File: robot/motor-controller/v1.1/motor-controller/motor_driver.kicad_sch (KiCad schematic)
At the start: 76 parts, among them J2 BM03B-ACHFKS, J4 BM06B-ACHFKS, J6 Conn_ARM_JTAG_SWD_10, Q1 STL90N10F7, Q2 STL90N10F7, Q3 STL90N10F7, Q4 STL90N10F7, Q5 STL90N10F7, Q6 STL90N10F7, Q7 BSS138K, U1 STSPIN32F0B, Y1 Q13FC13500005, Y2 TAXM8M4RDBCCT2T

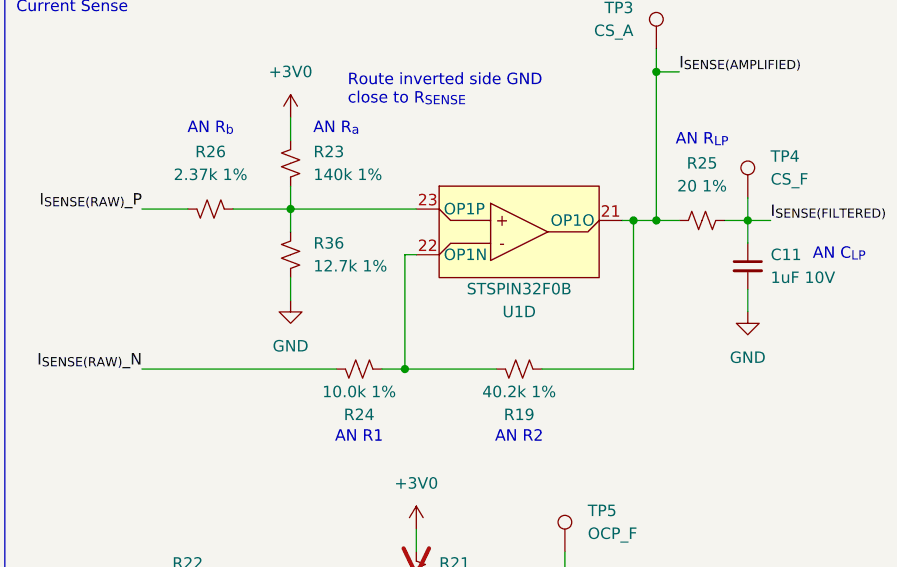
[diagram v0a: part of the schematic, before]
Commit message: fixed amplifier schematic
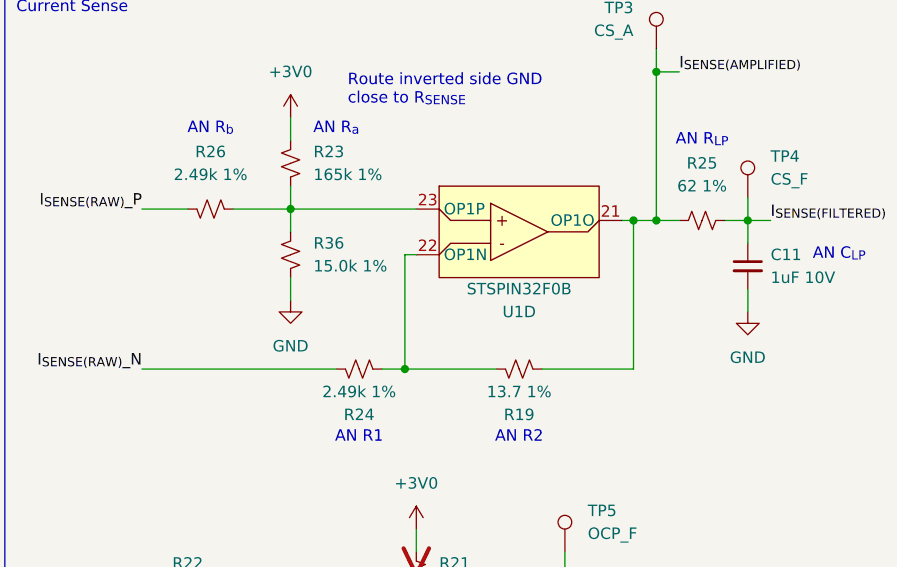
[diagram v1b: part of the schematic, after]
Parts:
- R19: value 40.2k 1% -> 13.7 1%
- R23: value 140k 1% -> 165k 1%
- R24: value 10.0k 1% -> 2.49k 1%
- R25: value 20 1% -> 62 1%
- R26: value 2.37k 1% -> 2.49k 1%
- R36: value 12.7k 1% -> 15.0k 1%
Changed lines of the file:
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@@
 			)
 		)
-		(property "Value" "20 1%"
+		(property "Value" "62 1%"
 			(at 316.23 168.91 90)
 			(effects
@@
 			)
 		)
-		(property "Value" "12.7k 1%"
+		(property "Value" "15.0k 1%"
 			(at 273.05 177.7999 0)
 			(effects
@@
 			)
 		)
-		(property "Value" "40.2k 1%"
+		(property "Value" "13.7 1%"
 			(at 295.91 191.77 90)
 			(effects
@@
 			)
 		)
-		(property "Value" "10.0k 1%"
+		(property "Value" "2.49k 1%"
 			(at 278.13 191.77 90)
 			(effects
@@
 			)
 		)
-		(property "Value" "2.37k 1%"
+		(property "Value" "2.49k 1%"
 			(at 261.62 167.64 90)
 			(effects
@@
 			)
 		)
-		(property "Value" "140k 1%"
+		(property "Value" "165k 1%"
 			(at 273.05 167.6399 0)
 			(effects

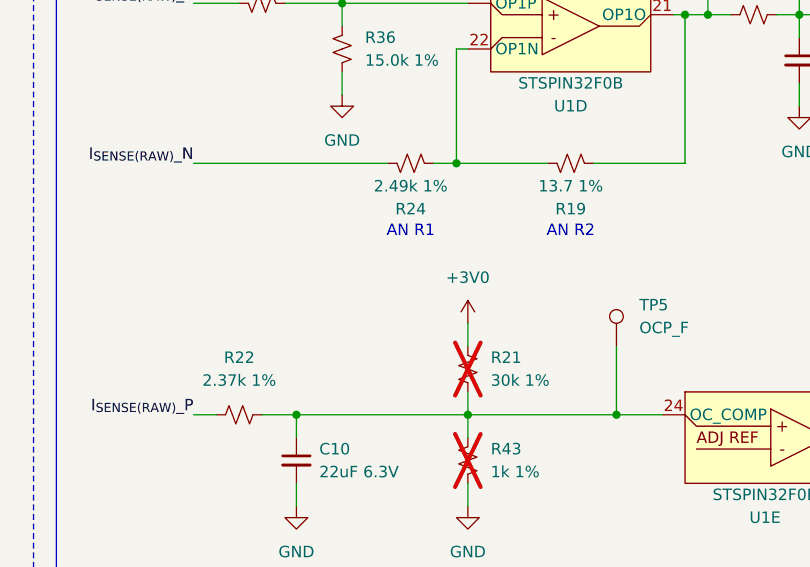
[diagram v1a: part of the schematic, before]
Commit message: BoM tweaks for prod
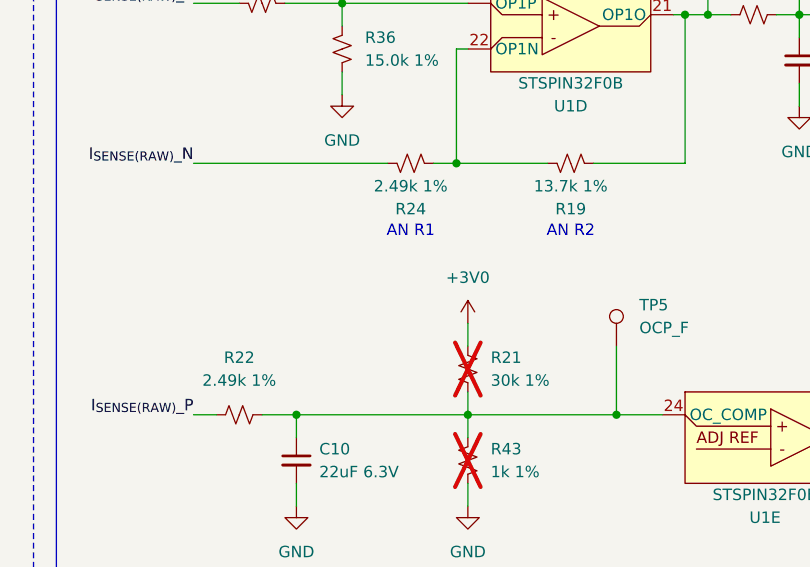
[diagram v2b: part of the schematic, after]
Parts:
- R19: value 13.7 1% -> 13.7k 1%
- R22: value 2.37k 1% -> 2.49k 1%
- TP1, TP2, TP3, TP4, TP5: now left out of the parts list
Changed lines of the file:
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@@
 		(unit 1)
 		(exclude_from_sim no)
-		(in_bom yes)
+		(in_bom no)
 		(on_board yes)
 		(dnp no)
@@
 		(unit 1)
 		(exclude_from_sim no)
-		(in_bom yes)
+		(in_bom no)
 		(on_board yes)
 		(dnp no)
@@
 			)
 		)
-		(property "Value" "2.37k 1%"
+		(property "Value" "2.49k 1%"
 			(at 259.08 213.36 90)
 			(effects
@@
 			)
 		)
-		(property "Value" "13.7 1%"
+		(property "Value" "13.7k 1%"
 			(at 295.91 191.77 90)
 			(effects
@@
 		(unit 1)
 		(exclude_from_sim no)
-		(in_bom yes)
+		(in_bom no)
 		(on_board yes)
 		(dnp no)
@@
 		(unit 1)
 		(exclude_from_sim no)
-		(in_bom yes)
+		(in_bom no)
 		(on_board yes)
 		(dnp no)
@@
 		(unit 1)
 		(exclude_from_sim no)
-		(in_bom yes)
+		(in_bom no)
 		(on_board yes)
 		(dnp no)

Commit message: BoM updated
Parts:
- C20, C21: LCSC C710643 -> C161525
- F4: LCSC (none) -> C377220
- J2: LCSC (none) -> C5177195
- J4: LCSC (none) -> C5304907
- R12, R13, R2, R3, R6, R9: LCSC C4962 -> C100501
- R19: LCSC C137983 -> C25854
- R21: LCSC C477764 -> C25776
- R22, R26: LCSC C25881 -> C25884
- R23: LCSC C852528 -> C38706
- R24: LCSC C60490 -> C25884
- R25: LCSC C138031 -> C100501
- R36: LCSC C852509 -> C2909322
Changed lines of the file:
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@@
 			)
 		)
+		(property "LCSC" "C5304907"
+			(at 182.88 176.53 0)
+			(effects
+				(font
+					(size 1.27 1.27)
+				)
+				(hide yes)
+			)
+		)
 		(pin "4"
 		)
@@
 			)
 		)
+		(property "LCSC" "C5177195"
+			(at 213.36 176.53 0)
+			(effects
+				(font
+					(size 1.27 1.27)
+				)
+				(hide yes)
+			)
+		)
 		(pin "2"
 		)
@@
 			)
 		)
-		(property "LCSC" "C4962"
+		(property "LCSC" "C100501"
 			(at 72.39 231.14 0)
 			(effects
@@
 			)
 		)
-		(property "LCSC" "C138031"
+		(property "LCSC" "C100501"
 			(at 316.23 166.37 0)
 			(effects
@@
 			)
 		)
-		(property "LCSC" "C25881"
+		(property "LCSC" "C25884"
 			(at 259.08 210.82 0)
 			(effects
@@
 			)
 		)
-		(property "LCSC" "C852509"
+		(property "LCSC" "C2909322"
 			(at 273.05 175.2599 0)
 			(effects
@@
 			)
 		)
-		(property "LCSC" "C137983"
+		(property "LCSC" "C25854"
 			(at 295.91 194.31 0)
 			(effects
@@
 			)
 		)
-		(property "LCSC" "C477764"
+		(property "LCSC" "C25776"
 			(at 287.02 210.8199 0)
 			(effects
@@
 			)
 		)
-		(property "LCSC" "C4962"
+		(property "LCSC" "C100501"
 			(at 72.39 198.12 0)
 			(effects
@@
 			)
 		)
-		(property "LCSC" "C4962"
+		(property "LCSC" "C100501"
 			(at 72.39 170.18 0)
 			(effects
@@
 			)
 		)
-		(property "LCSC" "C60490"
+		(property "LCSC" "C25884"
 			(at 278.13 194.31 0)
 			(effects
@@
 			)
 		)
-		(property "LCSC" "C710643"
+		(property "LCSC" "C161525"
 			(at 367.03 214.63 0)
 			(effects
@@
 			)
 		)
+		(property "LCSC" "C377220"
+			(at 50.8 59.69 0)
+			(effects
+				(font
+					(size 1.27 1.27)
+				)
+				(hide yes)
+			)
+		)
 		(pin "2"
 		)
@@
 			)
 		)
-		(property "LCSC" "C710643"
+		(property "LCSC" "C161525"
 			(at 392.43 214.63 0)
 			(effects
@@
 			)
 		)
-		(property "LCSC" "C4962"
+		(property "LCSC" "C100501"
 			(at 72.39 226.06 0)
 			(effects
@@
 			)
 		)
-		(property "LCSC" "C4962"
+		(property "LCSC" "C100501"
 			(at 72.39 175.26 0)
 			(effects
@@
 			)
 		)
-		(property "LCSC" "C4962"
+		(property "LCSC" "C100501"
 			(at 72.39 203.2 0)
 			(effects
@@
 			)
 		)
-		(property "LCSC" "C25881"
+		(property "LCSC" "C25884"
 			(at 261.62 165.1 0)
 			(effects
@@
 			)
 		)
-		(property "LCSC" "C852528"
+		(property "LCSC" "C38706"
 			(at 273.05 165.0999 0)
 			(effects

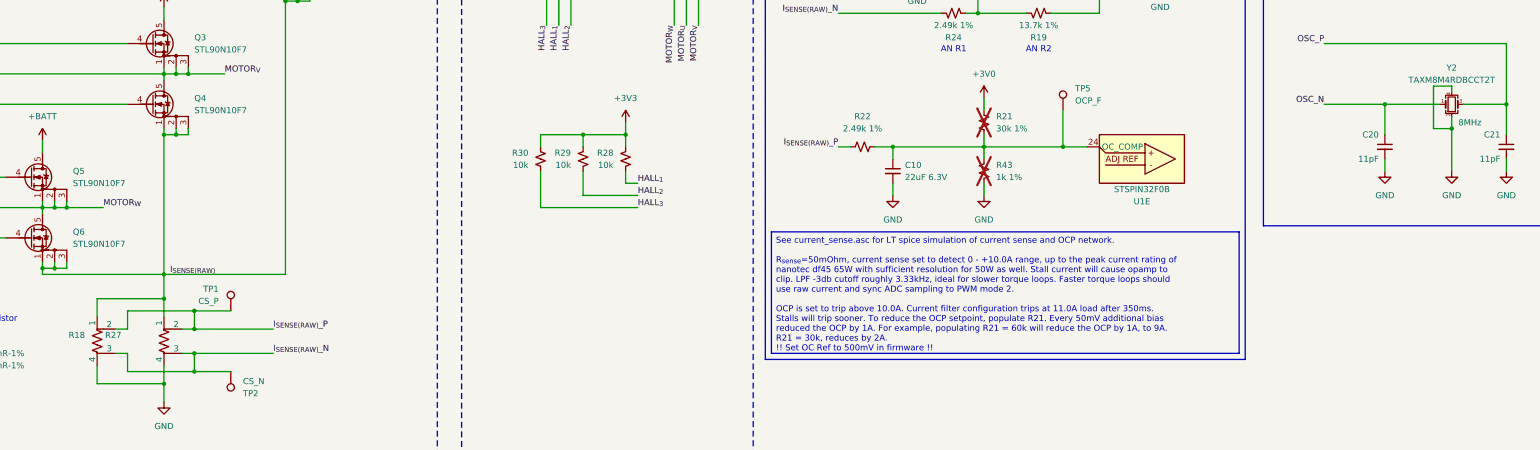
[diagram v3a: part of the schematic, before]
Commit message: minor tweaks to pass DRC with courtyard updates, fab products
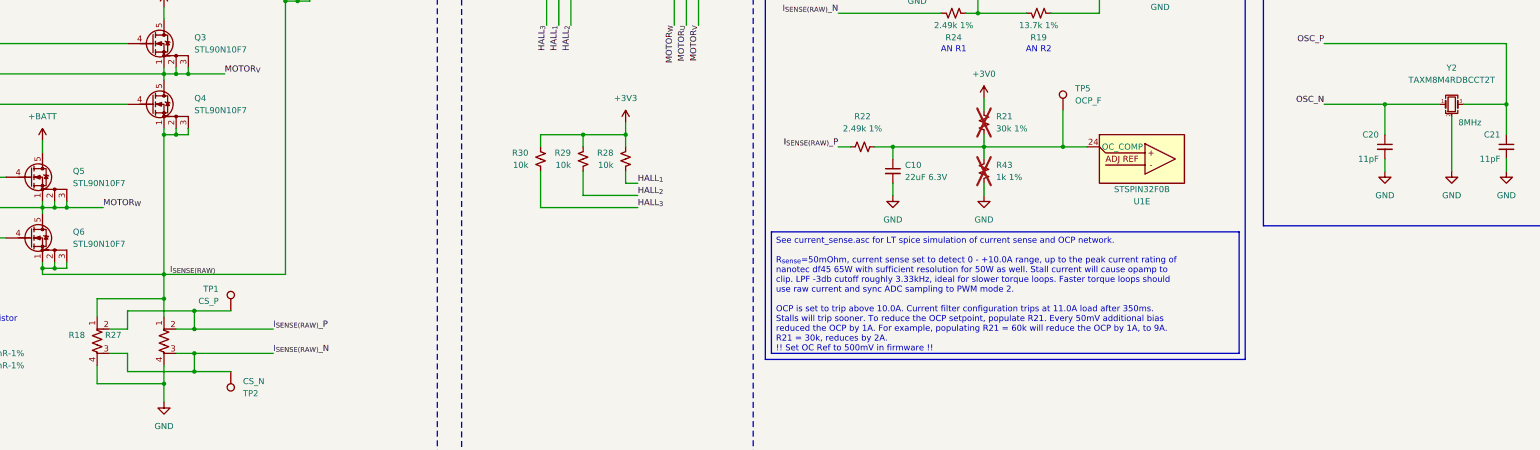
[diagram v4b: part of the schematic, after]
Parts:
- R19: LCSC C25854 -> C852522
- R22, R24, R26: LCSC C25884 -> C852700
- R23: LCSC C38706 -> C1509613
- R25: LCSC C100501 -> C852875
- R36: LCSC C2909322 -> C853539
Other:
- moved on the sheet: R18, R27
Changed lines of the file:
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@@
 	)
 	(junction
-		(at 382.27 213.36)
-		(diameter 0)
-		(color 0 0 0 0)
-	)
-	(junction
 		(at 308.61 172.72)
 		(diameter 0)
@@
 	(wire
 		(pts
-			(xy 102.87 260.35) (xy 105.41 260.35)
-		)
-		(stroke
-			(width 0)
-			(type default)
-		)
-	)
-	(wire
-		(pts
 			(xy 248.92 105.41) (xy 255.27 105.41)
 		)
@@
 	(wire
 		(pts
-			(xy 378.46 213.36) (xy 382.27 213.36)
-		)
-		(stroke
-			(width 0)
-			(type default)
-		)
-	)
-	(wire
-		(pts
 			(xy 219.71 39.37) (xy 257.81 39.37)
 		)
@@
 	(wire
 		(pts
-			(xy 382.27 205.74) (xy 382.27 204.47)
+			(xy 101.6 260.35) (xy 105.41 260.35)
 		)
 		(stroke
@@
 	(wire
 		(pts
-			(xy 382.27 213.36) (xy 382.27 222.25)
-		)
-		(stroke
-			(width 0)
-			(type default)
-		)
-	)
-	(wire
-		(pts
 			(xy 254 171.45) (xy 259.08 171.45)
 		)
@@
 	(wire
 		(pts
-			(xy 382.27 204.47) (xy 378.46 204.47)
-		)
-		(stroke
-			(width 0)
-			(type default)
-		)
-	)
-	(wire
-		(pts
 			(xy 379.73 109.22) (xy 388.62 109.22)
 		)
@@
 	(wire
 		(pts
-			(xy 382.27 210.82) (xy 382.27 213.36)
+			(xy 382.27 210.82) (xy 382.27 222.25)
 		)
 		(stroke
@@
 	(wire
 		(pts
-			(xy 378.46 204.47) (xy 378.46 213.36)
-		)
-		(stroke
-			(width 0)
-			(type default)
-		)
-	)
-	(wire
-		(pts
 			(xy 88.9 71.12) (xy 101.6 71.12)
 		)
@@
 	(wire
 		(pts
+			(xy 101.6 255.27) (xy 105.41 255.27)
+		)
+		(stroke
+			(width 0)
+			(type default)
+		)
+	)
+	(wire
+		(pts
 			(xy 90.17 228.6) (xy 90.17 229.87)
 		)
@@
 	(wire
 		(pts
-			(xy 102.87 255.27) (xy 105.41 255.27)
-		)
-		(stroke
-			(width 0)
-			(type default)
-		)
-	)
-	(wire
-		(pts
 			(xy 113.03 243.84) (xy 87.63 243.84)
 		)
@@
 	(wire
 		(pts
-			(xy 116.84 260.35) (xy 119.38 260.35)
+			(xy 115.57 260.35) (xy 119.38 260.35)
 		)
 		(stroke
@@
 	(wire
 		(pts
-			(xy 116.84 255.27) (xy 119.38 255.27)
-		)
-		(stroke
-			(width 0)
-			(type default)
-		)
-	)
-	(wire
-		(pts
 			(xy 200.66 182.88) (xy 200.66 180.34)
 		)
@@
 	(wire
 		(pts
+			(xy 115.57 255.27) (xy 119.38 255.27)
+		)
+		(stroke
+			(width 0)
+			(type default)
+		)
+	)
+	(wire
+		(pts
 			(xy 284.48 224.79) (xy 284.48 227.33)
 		)
@@
 		)
 		(instances
-			(project ""
+			(project "motor-controller"
 				(path "/128aa784-6ac2-4038-a52f-4d25824b8edd/cc912fad-bd7a-44ed-8392-4f59afec85c9"
 					(reference "J4")
@@
 		)
 		(instances
-			(project ""
+			(project "motor-controller"
 				(path "/128aa784-6ac2-4038-a52f-4d25824b8edd/cc912fad-bd7a-44ed-8392-4f59afec85c9"
 					(reference "J2")
@@
 			)
 		)
-		(property "Description" "Shunt resistor, US symbol"
+		(property "Description" "Shunt resistor with Kelvin connections, US symbol"
 			(at 99.06 257.81 0)
 			(effects
@@
 			)
 		)
-		(property "LCSC" "C100501"
+		(property "LCSC" "C852875"
 			(at 316.23 166.37 0)
 			(effects
@@
 			)
 		)
-		(property "LCSC" "C25884"
+		(property "LCSC" "C852700"
 			(at 259.08 210.82 0)
 			(effects
@@
 			)
 		)
-		(property "LCSC" "C2909322"
+		(property "LCSC" "C853539"
 			(at 273.05 175.2599 0)
 			(effects
@@
 			)
 		)
-		(property "LCSC" "C25854"
+		(property "LCSC" "C852522"
 			(at 295.91 194.31 0)
 			(effects
@@
 		)
 		(instances
-			(project ""
+			(project "motor-controller"
 				(path "/128aa784-6ac2-4038-a52f-4d25824b8edd/cc912fad-bd7a-44ed-8392-4f59afec85c9"
 					(reference "TP1")
@@
 		)
 		(instances
-			(project ""
+			(project "motor-controller"
 				(path "/128aa784-6ac2-4038-a52f-4d25824b8edd/cc912fad-bd7a-44ed-8392-4f59afec85c9"
 					(reference "C22")
@@
 			)
 		)
-		(property "Description" "Shunt resistor, US symbol"
+		(property "Description" "Shunt resistor with Kelvin connections, US symbol"
 			(at 113.03 257.81 0)
 			(effects
@@
 		)
 		(instances
-			(project ""
+			(project "motor-controller"
 				(path "/128aa784-6ac2-4038-a52f-4d25824b8edd/cc912fad-bd7a-44ed-8392-4f59afec85c9"
 					(reference "R27")
@@
 		)
 		(instances
-			(project ""
+			(project "motor-controller"
 				(path "/128aa784-6ac2-4038-a52f-4d25824b8edd/cc912fad-bd7a-44ed-8392-4f59afec85c9"
 					(reference "#PWR01")
@@
 			)
 		)
-		(property "LCSC" "C25884"
+		(property "LCSC" "C852700"
 			(at 278.13 194.31 0)
 			(effects
@@
 			)
 		)
-		(property "LCSC" "C25884"
+		(property "LCSC" "C852700"
 			(at 261.62 165.1 0)
 			(effects
@@
 			)
 		)
-		(property "LCSC" "C38706"
+		(property "LCSC" "C1509613"
 			(at 273.05 165.0999 0)
 			(effects
